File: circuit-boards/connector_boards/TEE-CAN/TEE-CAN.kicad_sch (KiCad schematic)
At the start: 6 parts, among them J1 Conn_01x02_Pin, J2 Conn_01x02_Pin, J3 Conn_01x02_Pin, J4 Conn_01x02_Pin

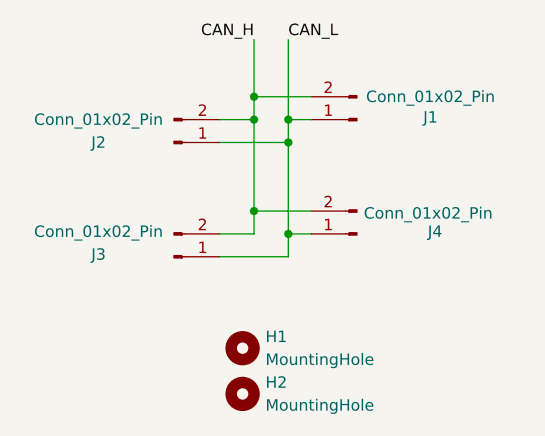
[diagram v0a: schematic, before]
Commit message: Add new boms (gold-plated tee-can)etc
Signed-off-by: Alex lenkov <Alexander.i.lenkov@gmail.com>
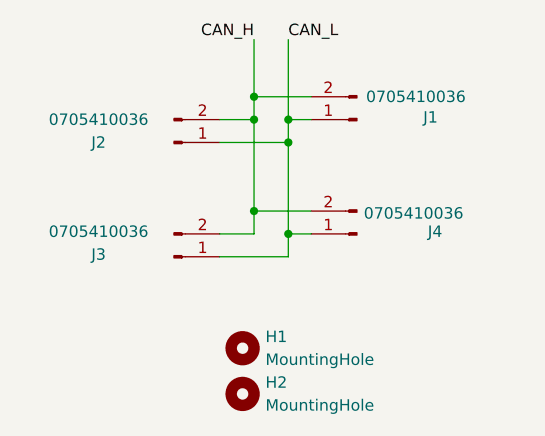
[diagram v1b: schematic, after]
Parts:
- J1, J2, J3, J4: value Conn_01x02_Pin -> 0705410036; DIST (none) -> DIGIKEY; DIST P/N (none) -> WM14049-ND; MFG (none) -> MOLEX; MFG P/N (none) -> 0705410036
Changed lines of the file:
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@@
 		)
 		(instances
-			(project "Sl-Can"
+			(project "TEE-CAN"
 				(path "/550ab8e1-338b-4617-8ac4-8a8001411a88"
 					(reference "H2")
@@
 			)
 		)
-		(property "Value" "Conn_01x02_Pin"
+		(property "Value" "0705410036"
 			(at 113.792 73.914 0)
 			(effects
@@
 			)
 		)
-		(property "Datasheet" "~"
+		(property "Datasheet" "Components/PS-70400.pdf"
 			(at 113.03 76.2 0)
 			(effects
@@
 			)
 		)
+		(property "DIST" "DIGIKEY"
+			(at 113.03 76.2 0)
+			(effects
+				(font
+					(size 1.27 1.27)
+				)
+				(hide yes)
+			)
+		)
+		(property "DIST P/N" "WM14049-ND"
+			(at 113.03 76.2 0)
+			(effects
+				(font
+					(size 1.27 1.27)
+				)
+				(hide yes)
+			)
+		)
+		(property "MFG" "MOLEX"
+			(at 113.03 76.2 0)
+			(effects
+				(font
+					(size 1.27 1.27)
+				)
+				(hide yes)
+			)
+		)
+		(property "MFG P/N" "0705410036"
+			(at 113.03 76.2 0)
+			(effects
+				(font
+					(size 1.27 1.27)
+				)
+				(hide yes)
+			)
+		)
 		(pin "2"
 		)
@@
 		)
 		(instances
-			(project "Sl-Can"
+			(project "TEE-CAN"
 				(path "/550ab8e1-338b-4617-8ac4-8a8001411a88"
 					(reference "J4")
@@
 			)
 		)
-		(property "Value" "Conn_01x02_Pin"
+		(property "Value" "0705410036"
 			(at 84.328 63.5 0)
 			(effects
@@
 			)
 		)
-		(property "Datasheet" "~"
+		(property "Datasheet" "Components/PS-70400.pdf"
 			(at 92.71 66.04 0)
 			(effects
@@
 			)
 		)
+		(property "DIST" "DIGIKEY"
+			(at 92.71 66.04 0)
+			(effects
+				(font
+					(size 1.27 1.27)
+				)
+				(hide yes)
+			)
+		)
+		(property "DIST P/N" "WM14049-ND"
+			(at 92.71 66.04 0)
+			(effects
+				(font
+					(size 1.27 1.27)
+				)
+				(hide yes)
+			)
+		)
+		(property "MFG" "MOLEX"
+			(at 92.71 66.04 0)
+			(effects
+				(font
+					(size 1.27 1.27)
+				)
+				(hide yes)
+			)
+		)
+		(property "MFG P/N" "0705410036"
+			(at 92.71 66.04 0)
+			(effects
+				(font
+					(size 1.27 1.27)
+				)
+				(hide yes)
+			)
+		)
 		(pin "2"
 		)
@@
 		)
 		(instances
-			(project "Sl-Can"
+			(project "TEE-CAN"
 				(path "/550ab8e1-338b-4617-8ac4-8a8001411a88"
 					(reference "J2")
@@
 			)
 		)
-		(property "Value" "Conn_01x02_Pin"
+		(property "Value" "0705410036"
 			(at 84.328 75.946 0)
 			(effects
@@
 			)
 		)
-		(property "Datasheet" "~"
-			(at 92.71 78.74 0)
-			(effects
-				(font
-					(size 1.27 1.27)
-				)
-				(hide yes)
-			)
-		)
-		(property "Description" "Generic connector, single row, 01x02, script generated"
+		(property "Datasheet" "Components/PS-70400.pdf"
+			(at 92.71 78.74 0)
+			(effects
+				(font
+					(size 1.27 1.27)
+				)
+				(hide yes)
+			)
+		)
+		(property "Description" "2 Pin"
+			(at 92.71 78.74 0)
+			(effects
+				(font
+					(size 1.27 1.27)
+				)
+				(hide yes)
+			)
+		)
+		(property "MFG" "MOLEX"
+			(at 92.71 78.74 0)
+			(effects
+				(font
+					(size 1.27 1.27)
+				)
+				(hide yes)
+			)
+		)
+		(property "MFG P/N" "0705410036"
+			(at 92.71 78.74 0)
+			(effects
+				(font
+					(size 1.27 1.27)
+				)
+				(hide yes)
+			)
+		)
+		(property "DIST" "DIGIKEY"
+			(at 92.71 78.74 0)
+			(effects
+				(font
+					(size 1.27 1.27)
+				)
+				(hide yes)
+			)
+		)
+		(property "DIST P/N" "WM14049-ND"
 			(at 92.71 78.74 0)
 			(effects
@@
 		)
 		(instances
-			(project "Sl-Can"
+			(project "TEE-CAN"
 				(path "/550ab8e1-338b-4617-8ac4-8a8001411a88"
 					(reference "J3")
@@
 		)
 		(instances
-			(project "Sl-Can"
+			(project "TEE-CAN"
 				(path "/550ab8e1-338b-4617-8ac4-8a8001411a88"
 					(reference "H1")
@@
 			)
 		)
-		(property "Value" "Conn_01x02_Pin"
+		(property "Value" "0705410036"
 			(at 114.046 60.96 0)
 			(effects
@@
 			)
 		)
-		(property "Datasheet" "~"
+		(property "Datasheet" "Components/PS-70400.pdf"
 			(at 113.03 63.5 0)
 			(effects
@@
 			)
 		)
+		(property "DIST" "DIGIKEY"
+			(at 113.03 63.5 0)
+			(effects
+				(font
+					(size 1.27 1.27)
+				)
+				(hide yes)
+			)
+		)
+		(property "DIST P/N" "WM14049-ND"
+			(at 113.03 63.5 0)
+			(effects
+				(font
+					(size 1.27 1.27)
+				)
+				(hide yes)
+			)
+		)
+		(property "MFG" "MOLEX"
+			(at 113.03 63.5 0)
+			(effects
+				(font
+					(size 1.27 1.27)
+				)
+				(hide yes)
+			)
+		)
+		(property "MFG P/N" "0705410036"
+			(at 113.03 63.5 0)
+			(effects
+				(font
+					(size 1.27 1.27)
+				)
+				(hide yes)
+			)
+		)
 		(pin "2"
 		)
@@
 		)
 		(instances
-			(project "Sl-Can"
+			(project "TEE-CAN"
 				(path "/550ab8e1-338b-4617-8ac4-8a8001411a88"
 					(reference "J1")
